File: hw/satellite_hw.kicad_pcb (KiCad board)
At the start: 2 copper layers, 43.7 x 21.1 mm, 21 parts, among them J1 solar 1, J2 solar 2, J3 solar 3, J4 solar 4, Q1 2N7002, U1 AP3015, U2 ATtiny13-20SU

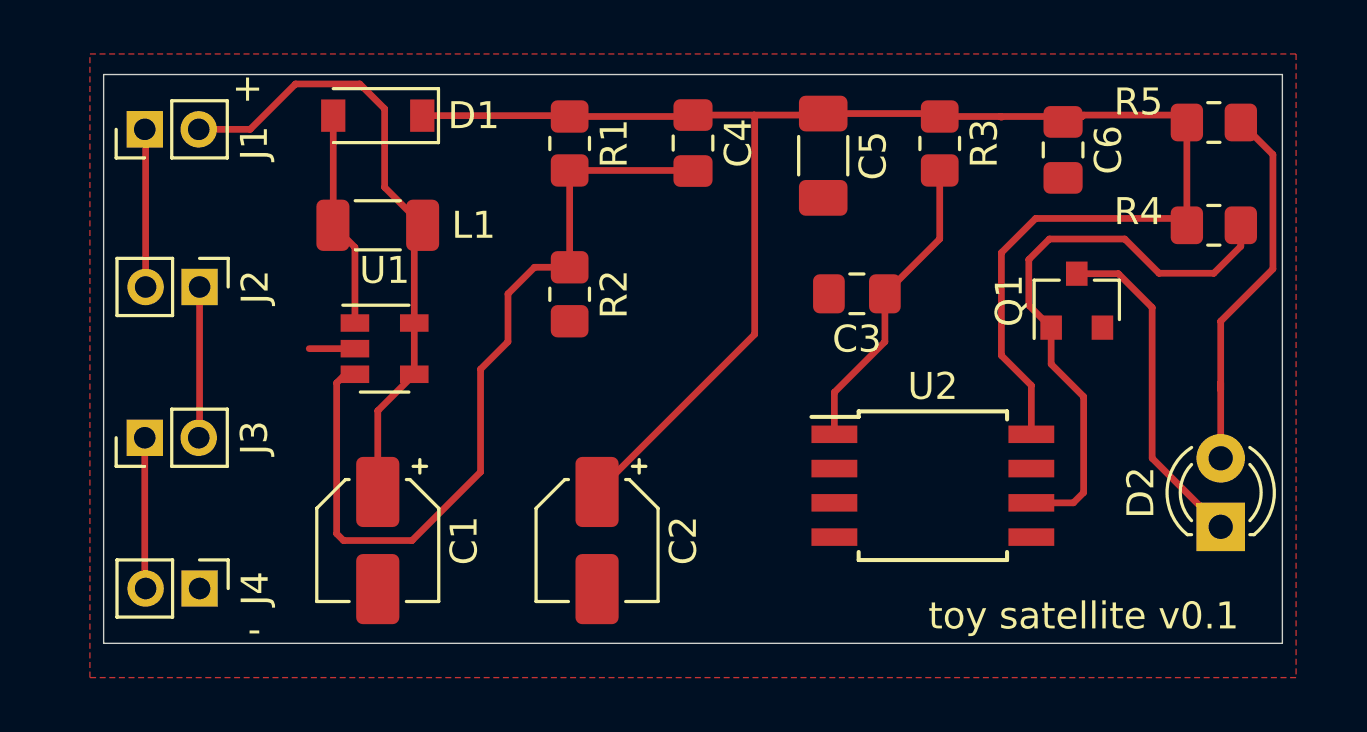
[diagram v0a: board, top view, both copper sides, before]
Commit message: fixed pinheaders to math with typical goldpins
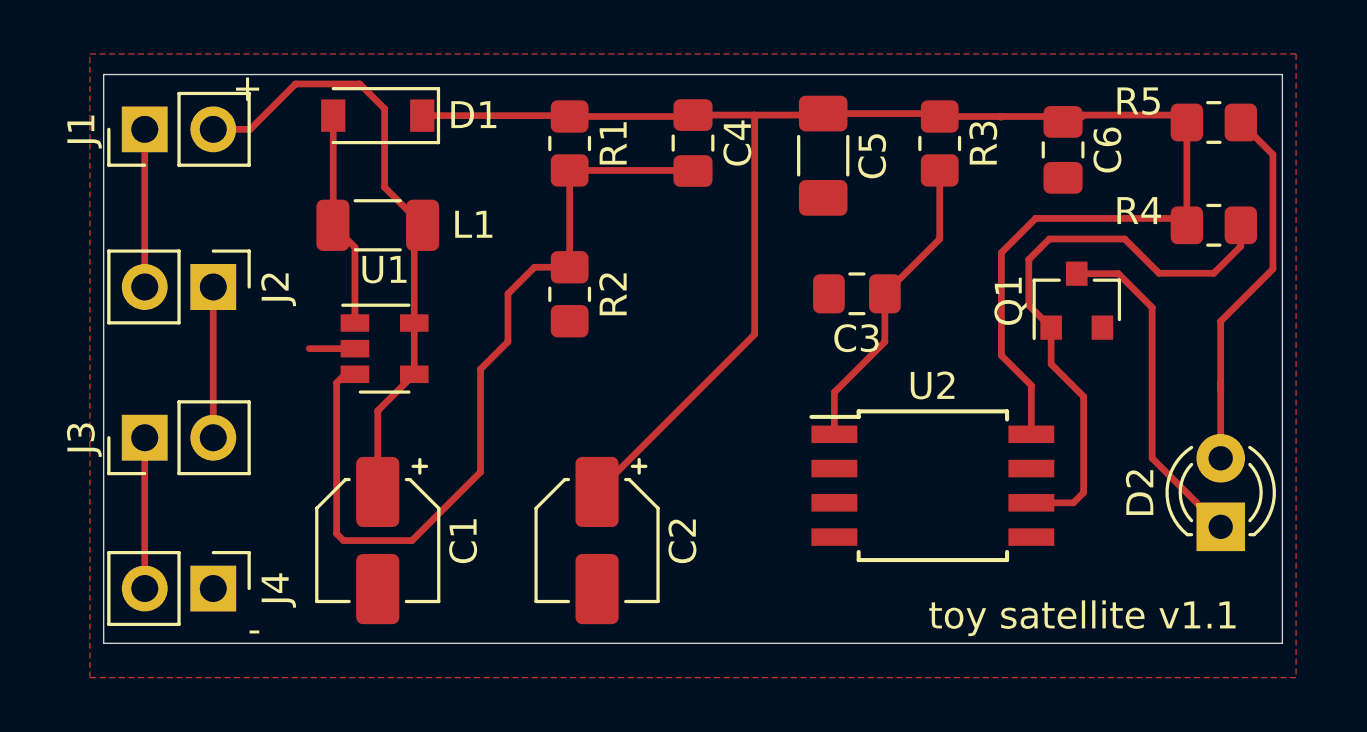
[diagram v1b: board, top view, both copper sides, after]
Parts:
- J1, J2, J3, J4: footprint Connector_PinHeader_2.00mm:PinHeader_1x02_P2.00mm_Vertical -> Connector_PinHeader_2.54mm:PinHeader_1x02_P2.54mm_Vertical
- moved J2 0.51 mm to (98.6, 80.5)
- moved J4 0.51 mm to (98.6, 91.7)
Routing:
- net VCC: track 23.4 -> 22.9 mm
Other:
- board text added: "toy satellite v1.1"
- board text removed: "toy satellite v0.1"
